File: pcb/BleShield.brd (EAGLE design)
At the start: 11 parts, among them U1 ARDUINO_SHIELDNOHOLES, Y1 32.768KHz, 10PPM

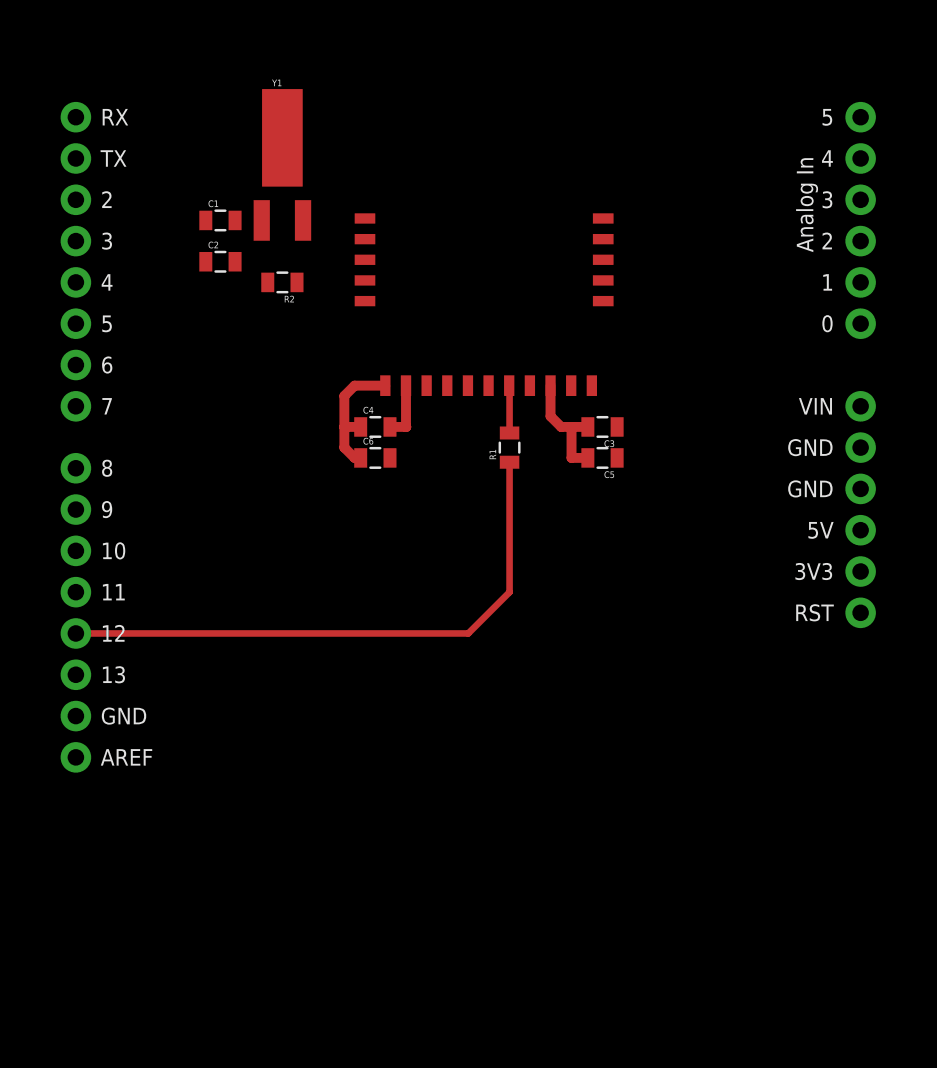
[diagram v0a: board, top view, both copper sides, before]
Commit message: Add option to use software serial port, make the board smaller, etc.
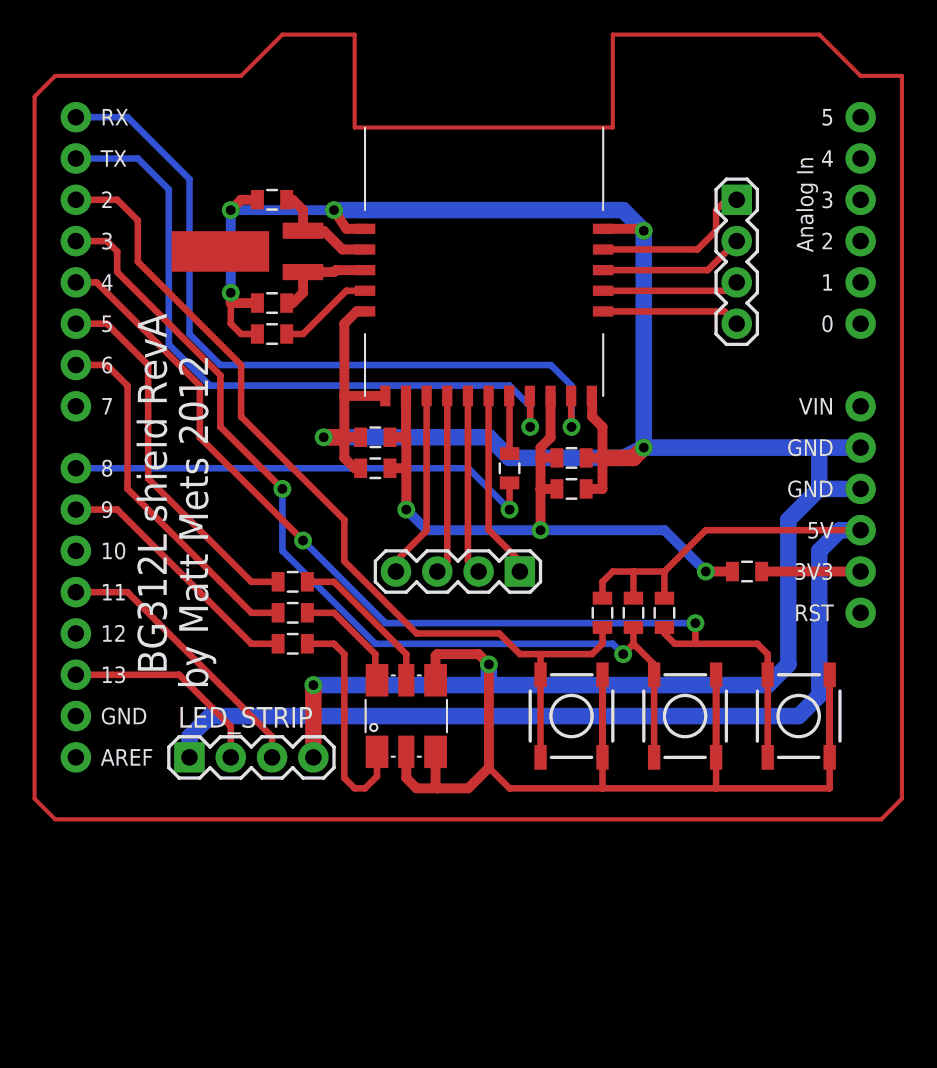
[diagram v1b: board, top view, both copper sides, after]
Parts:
- added JP1, JP2, LED_STRIP: (no value), SparkFun:1X04
- added LED4: LED-TRICOLOR-5050, SparkFun:LED-TRICOLOR-5050
- added R3, R4, R5: 330, SparkFun:0805
- added R6: 0, SparkFun:0805
- added R7, R8, R9: 10K, SparkFun:0805
- added S1, S2, S3: (no value), SparkFun:TACTILE_SWITCH_SMD
- moved C2 4.07 mm to (14.6, 43.2)
- moved C1 3.42 mm to (14.6, 49.5)
- moved R2 3.24 mm to (14.6, 41.3)
- moved C3 2.69 mm to (33.0, 33.7)
- moved C5 2.69 mm to (33.0, 31.8)
- moved Y1 2.29 mm to (16.5, 46.4), turned to 90 degrees
- moved R1 1.27 mm to (29.2, 33.0)
- moved C4 0.64 mm to (21.0, 34.9)
- moved C6 0.63 mm to (21.0, 33.0)
- moved U$1 0.63 mm to (20.3, 37.5)
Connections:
- new net 5V: LED_STRIP.1, R7.2, R8.2, R9.2, U1.5V
- new net LED_GREEN: R4.1, U1.D6
- new net LED_RED: R3.1, U1.D9
- new net MOSI: LED_STRIP.3, U1.D11
- new net N$10: JP1.2, U$1.P0_5
- new net N$11: JP1.3, U$1.P0_6
- new net N$12: JP1.4, U$1.P0_7
- new net N$13: JP2.1, U$1.P1_5/RT
- new net N$14: JP2.2, U$1.P1_4/CT
- new net N$15: JP2.3, U$1.P2_1
- new net N$16: JP2.4, U$1.P2_2
- new net N$5: LED4.2, R3.2
- new net N$6: LED4.1, R4.2
- new net N$7: LED4.3, R5.2
- new net N$8: C3.2, C4.2, C5.2, C6.2, R6.2, U$1.VDD_1, U$1.VDD_2
- new net N$9: JP1.1, U$1.P0_4
- new net PROP: R5.1, U1.D5
- new net SCK: LED_STRIP.2, U1.D13
- new net SWITCH_A: R7.1, S1.3, S1.4, U1.D2
- new net SWITCH_B: R8.1, S2.3, S2.4, U1.D3
- new net SWITCH_C: R9.1, S3.3, S3.4, U1.D4
- net 3.3V: now also R6.1; no longer C3.2, C4.2, C5.2, C6.2, U$1.VDD_1, U$1.VDD_2
- net GND: now also LED4.4, LED4.5, LED4.6, LED_STRIP.4, S1.1, S1.2, S2.1, S2.2, S3.1, S3.2
- net RESET: now also U1.D8; no longer U1.D12
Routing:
- net GND: track 8.23 -> 248.2 mm, vias 0 -> 8
- net N$17: track 0.00 -> 209.4 mm
- net 5V: track 0.00 -> 74.5 mm
- net SWITCH_C: track 0.00 -> 63.5 mm, vias 0 -> 2
- net SWITCH_B: track 0.00 -> 58.4 mm, vias 0 -> 2
- net SWITCH_A: track 0.00 -> 56.4 mm
- net RX: track 0.00 -> 47.3 mm, vias 0 -> 1
- net TX: track 0.00 -> 43.0 mm, vias 0 -> 1
- net N$8: track 0.00 -> 41.2 mm, vias 0 -> 3
- net PROP: track 0.00 -> 23.1 mm
- net LED_GREEN: track 0.00 -> 22.5 mm
- net MOSI: track 0.00 -> 17.0 mm
- net LED_RED: track 0.00 -> 15.9 mm
- net N$5: track 0.00 -> 14.2 mm
- net SCK: track 0.00 -> 12.7 mm
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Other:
- board text added: "BG312L shield RevA"
- board text added: "by Matt Mets 2012"

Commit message: label most of the things
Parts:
- added R10, R11: 0 DNP, SparkFun:0805
- added R12, R13: 0, SparkFun:0805
- JP0: value (none) -> LED_STRIP
- S1: value (none) -> A
- moved C1 1.27 mm to (14.6, 48.3)
- moved C2 1.27 mm to (14.6, 41.9)
- moved R2 1.27 mm to (14.6, 40.0)
- moved Y1 1.27 mm to (16.5, 45.1)
- renumbered LED_STRIP to JP0, S2 to B, S3 to C
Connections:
- net PROP renamed LED_BLUE
- new net N$18: R10.2, U1.D2
- new net N$19: R12.2, U1.RX
- new net N$20: R13.2, U1.TX
- new net N$21: R11.2, U1.D3
- net RX: now also R10.1, R12.1; no longer U1.RX
- net SWITCH_A: now also U1.D4; no longer U1.D2
- net SWITCH_B: now also U1.D12; no longer U1.D3
- net SWITCH_C: now also U1.D7; no longer U1.D4
- net TX: now also R11.1, R13.1; no longer U1.TX
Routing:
- net SWITCH_B: track 58.4 -> 44.1 mm, vias 2 -> 1
- net N$21: track 0.00 -> 4.44 mm
- net N$20: track 0.00 -> 4.44 mm
- net N$19: track 0.00 -> 4.18 mm
- net N$18: track 0.00 -> 4.18 mm
- net GND: track 248.2 -> 251.6 mm, vias 8 -> 7
- net SWITCH_A: track 56.4 -> 53.9 mm
- net SWITCH_C: track 63.5 -> 61.1 mm
- net TX: track 43.0 -> 41.7 mm, vias 1 -> 3
- net N$2: track 5.92 -> 7.19 mm
- net N$4: track 6.40 -> 6.92 mm
- net RX: track 47.3 -> 47.8 mm, vias 1 -> 2

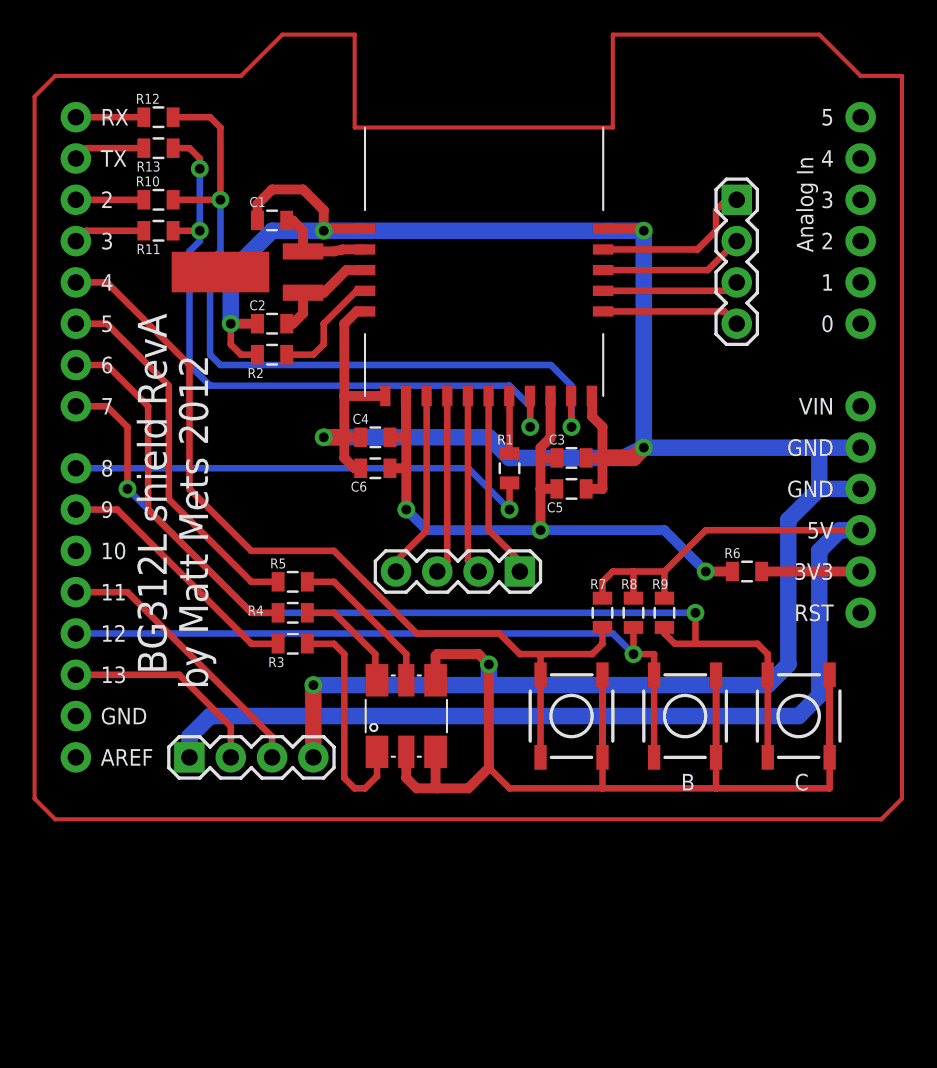
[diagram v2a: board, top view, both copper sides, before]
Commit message: RevA version, as shipped.
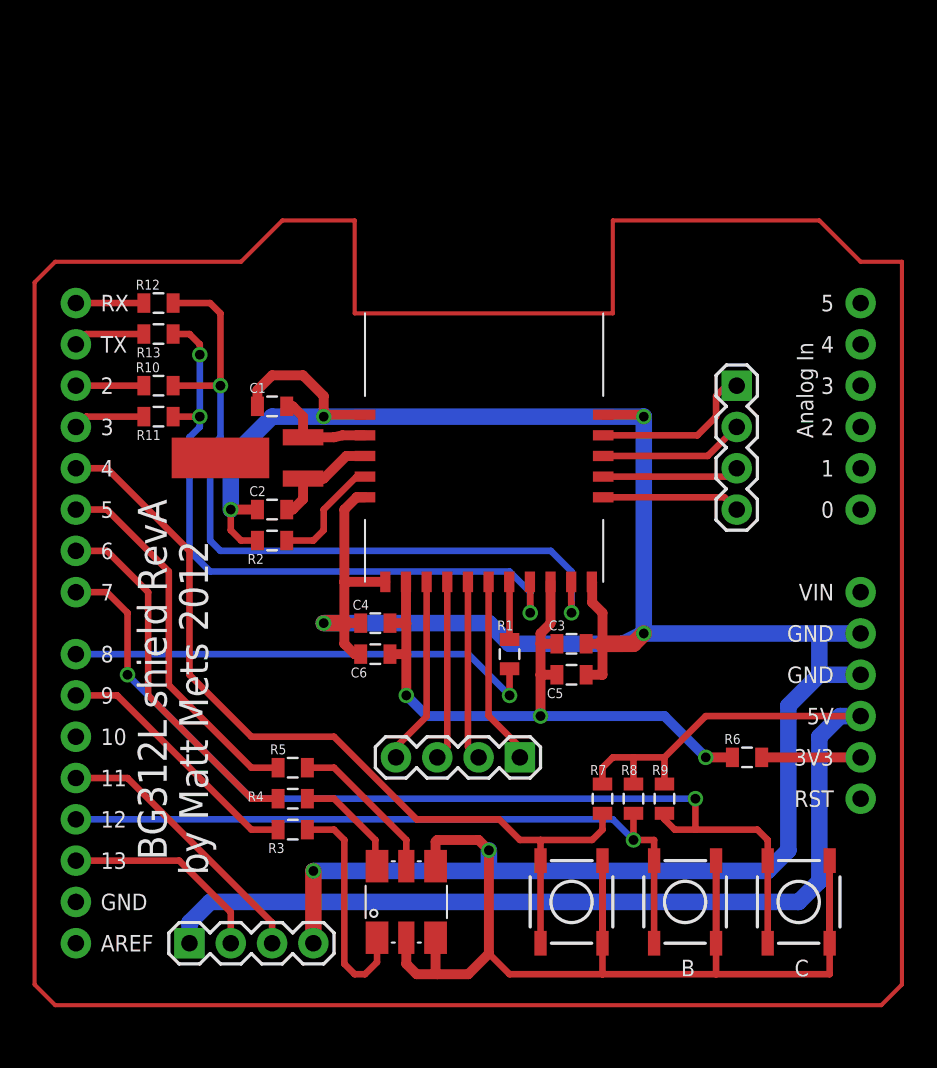
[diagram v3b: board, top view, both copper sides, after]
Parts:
- moved C6 11.4 mm to (21.0, 21.6)
- moved R1 11.4 mm to (29.2, 21.6)
- moved R2 11.4 mm to (14.6, 28.6)
- moved U$1 11.4 mm to (20.3, 26.0)
- moved B 11.4 mm to (40.0, 6.35)
- moved C 11.4 mm to (47.0, 6.35)
- moved JP2 11.4 mm to (29.8, 15.2)
- moved LED4 11.4 mm to (22.9, 6.35)
- moved R3 11.4 mm to (15.9, 10.8)
- moved R6 11.4 mm to (43.8, 15.2)
- moved S1 11.4 mm to (33.0, 6.35)
- moved C1 11.4 mm to (14.6, 36.8)
- moved C3 11.4 mm to (33.0, 22.2)
- moved C5 11.4 mm to (33.0, 20.3)
- moved JP0 11.4 mm to (9.53, 3.81)
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
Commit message: Remove R2 resistor
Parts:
- removed R2: 1K, SparkFun:0805
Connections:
- removed net N$2: R2.1, U$1.P2_0
- net GND: no longer R2.2
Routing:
- net N$2: track 7.19 -> 0.00 mm
- net GND: track 251.6 -> 248.4 mm
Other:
- board text added: "BG312L shield RevBpre"
- board text removed: "BG312L shield RevA"
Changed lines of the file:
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@@
 <?xml version="1.0" encoding="utf-8"?>
 <!DOCTYPE eagle SYSTEM "eagle.dtd">
-<eagle version="6.2">
+<eagle version="6.4">
 <drawing>
 <settings>
@@
 <board>
 <plain>
-<text x="6.35" y="31.115" size="1.778" layer="25" rot="R270">BG312L shield RevA</text>
+<text x="6.35" y="31.115" size="1.778" layer="25" rot="R270">BG312L shield RevBpre</text>
 <text x="8.89" y="28.575" size="1.778" layer="25" rot="R270">by Matt Mets 2012</text>
 </plain>
@@
 </class>
 </classes>
-<designrules>
+<designrules name="default">
 <description language="de">&lt;b&gt;EAGLE Design Rules&lt;/b&gt;
 &lt;p&gt;
@@
 <attribute name="NAME" x="28.448" y="23.0505" size="0.6096" layer="25"/>
 </element>
-<element name="R2" library="SparkFun" package="0805" value="1K" x="14.605" y="28.575" smashed="yes" rot="R180">
-<attribute name="NAME" x="14.097" y="27.7495" size="0.6096" layer="25" rot="R180"/>
-</element>
 <element name="C1" library="SparkFun" package="0805" value="15pf" x="14.605" y="36.83" smashed="yes">
 <attribute name="NAME" x="13.208" y="37.6555" size="0.6096" layer="25"/>
@@
 <contactref element="U$1" pad="GND_2"/>
 <contactref element="U$1" pad="GND_1"/>
-<contactref element="R2" pad="2"/>
 <contactref element="C1" pad="1"/>
 <contactref element="C2" pad="1"/>
@@
 <wire x1="12.065" y1="33.655" x2="14.605" y2="36.195" width="1.016" layer="16"/>
 <wire x1="14.605" y1="36.195" x2="17.78" y2="36.195" width="1.016" layer="16"/>
-<wire x1="13.705" y1="28.575" x2="12.7" y2="28.575" width="0.4064" layer="1"/>
-<wire x1="12.7" y1="28.575" x2="12.065" y2="29.21" width="0.4064" layer="1"/>
-<wire x1="12.065" y1="29.21" x2="12.065" y2="30.48" width="0.4064" layer="1"/>
+<wire x1="12.7" y1="28.575" x2="12.065" y2="29.21" width="0" layer="19" extent="1-16"/>
+<wire x1="12.065" y1="29.21" x2="12.065" y2="30.48" width="0" layer="19" extent="1-16"/>
 </signal>
 <signal name="N$1">
@@
 <wire x1="29.21" y1="26.035" x2="29.21" y2="22.49" width="0.4064" layer="1"/>
 </signal>
-<signal name="N$2">
-<contactref element="U$1" pad="P2_0"/>
-<contactref element="R2" pad="1"/>
-<wire x1="15.505" y1="28.575" x2="17.145" y2="28.575" width="0.4064" layer="1"/>
-<wire x1="20.32" y1="32.505" x2="19.805" y2="32.505" width="0.4064" layer="1"/>
-<wire x1="19.805" y1="32.505" x2="17.78" y2="30.48" width="0.4064" layer="1"/>
-<wire x1="17.78" y1="30.48" x2="17.78" y2="29.21" width="0.4064" layer="1"/>
-<wire x1="17.78" y1="29.21" x2="17.145" y2="28.575" width="0.4064" layer="1"/>
-</signal>
 <signal name="RESET">

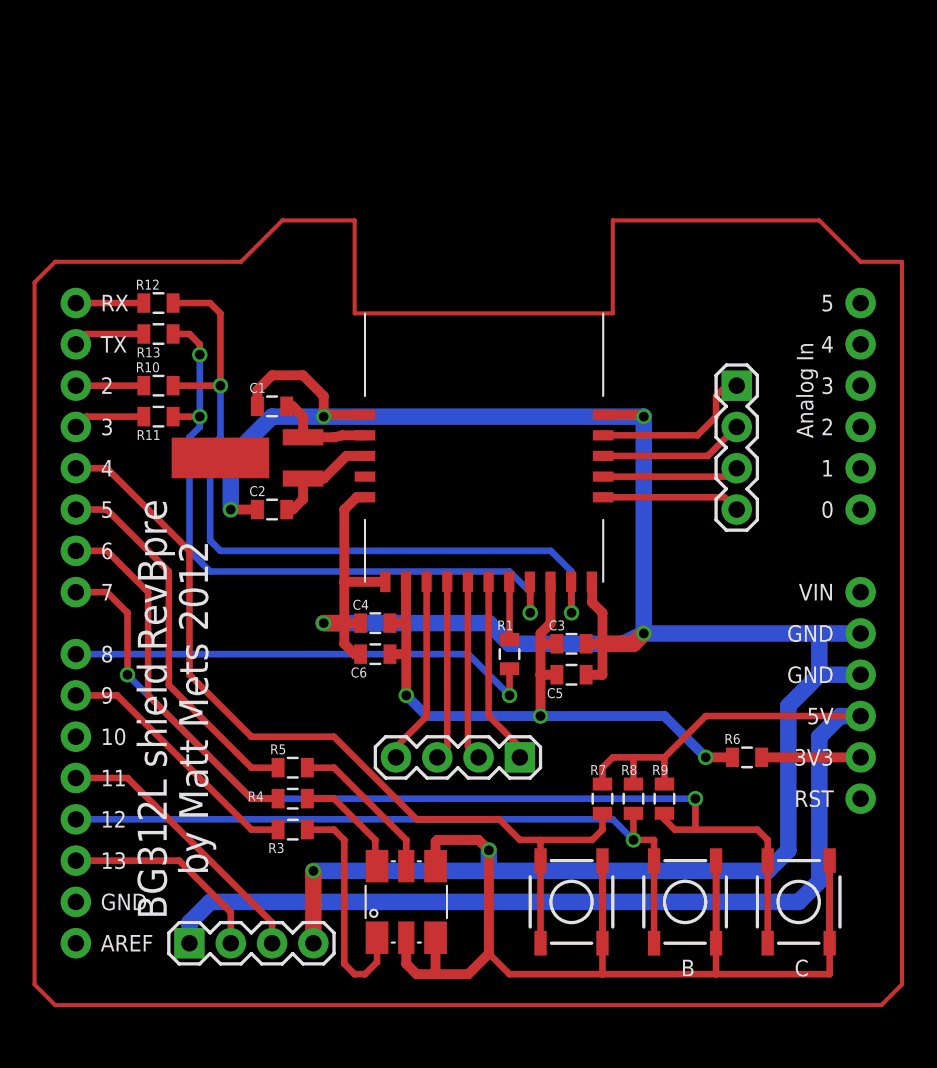
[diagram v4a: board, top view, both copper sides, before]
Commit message: fixed LED pinout, changed crystal to 3225 package
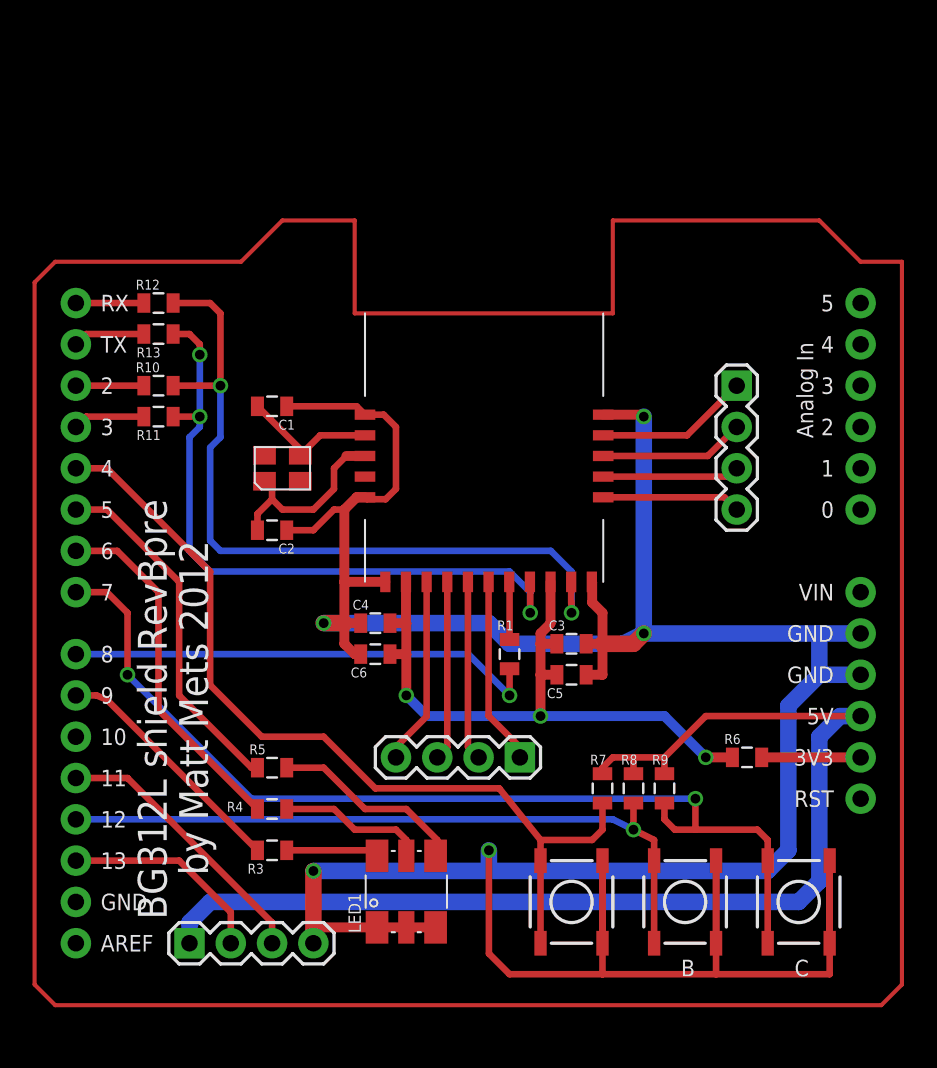
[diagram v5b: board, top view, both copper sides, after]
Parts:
- removed LED4: LED-TRICOLOR-5050, SparkFun:LED-TRICOLOR-5050
- added LED1: LED-TRICOLOR-5050", blinkiverse:LED-TRICOLOR-5050-FIXED
- Y1: value 32.768KHz, 10PPM -> 32.768KHz, 10 PPM; device SparkFun:CRYSTAL-32KHZ-SMD -> blinkiverse:XS3225
- moved R3 1.80 mm to (14.6, 9.53)
- moved Y1 1.42 mm to (15.2, 33.0), turned to 0 degrees
- moved R4 1.42 mm to (14.6, 12.1)
- moved C2 1.27 mm to (14.6, 29.2), turned to 180 degrees
- moved R5 1.27 mm to (14.6, 14.6)
- moved R7 0.64 mm to (34.9, 13.3)
- moved R8 0.64 mm to (36.8, 13.3)
- moved R9 0.64 mm to (38.7, 13.3)
- turned C1 to 180 degrees
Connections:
- removed net N$7: LED4.3, R5.2
- new net N$2: LED1.6, R3.2
- net GND: now also LED1.1, LED1.2, LED1.3; no longer LED4.4, LED4.5, LED4.6
- net LED_BLUE: now also R3.1, U1.D9; no longer R5.1, U1.D5
- net LED_GREEN: now also R5.1, U1.D5; no longer R4.1, U1.D6
- net LED_RED: now also R4.1, U1.D6; no longer R3.1, U1.D9
- net N$3: now also Y1.P$3; no longer Y1.X2
- net N$4: now also Y1.P$1; no longer Y1.X1
- net N$5: now also LED1.4, R5.2; no longer LED4.2, R3.2
- net N$6: now also LED1.5; no longer LED4.1
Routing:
- net GND: track 248.4 -> 217.8 mm, vias 7 -> 5
- net N$7: track 9.54 -> 0.00 mm
- net LED_BLUE: track 23.1 -> 15.1 mm
- net LED_RED: track 15.9 -> 22.0 mm
- net N$2: track 0.00 -> 5.70 mm
- net N$4: track 6.92 -> 11.7 mm
- net N$6: track 6.89 -> 9.12 mm
- net N$3: track 6.36 -> 8.59 mm
- net N$5: track 14.2 -> 12.1 mm
- net 5V: track 74.5 -> 72.6 mm
- net N$9: track 10.2 -> 9.48 mm
- net SWITCH_C: track 61.1 -> 61.7 mm
- net LED_GREEN: track 22.5 -> 21.8 mm
